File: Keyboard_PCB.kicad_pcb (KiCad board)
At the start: 2 copper layers, 21 parts, among them CON1 PS/2_JACK, CON2 USB_JACK, IC1 FT232RL, U1 ATMEGA328, X1 CRYSTAL

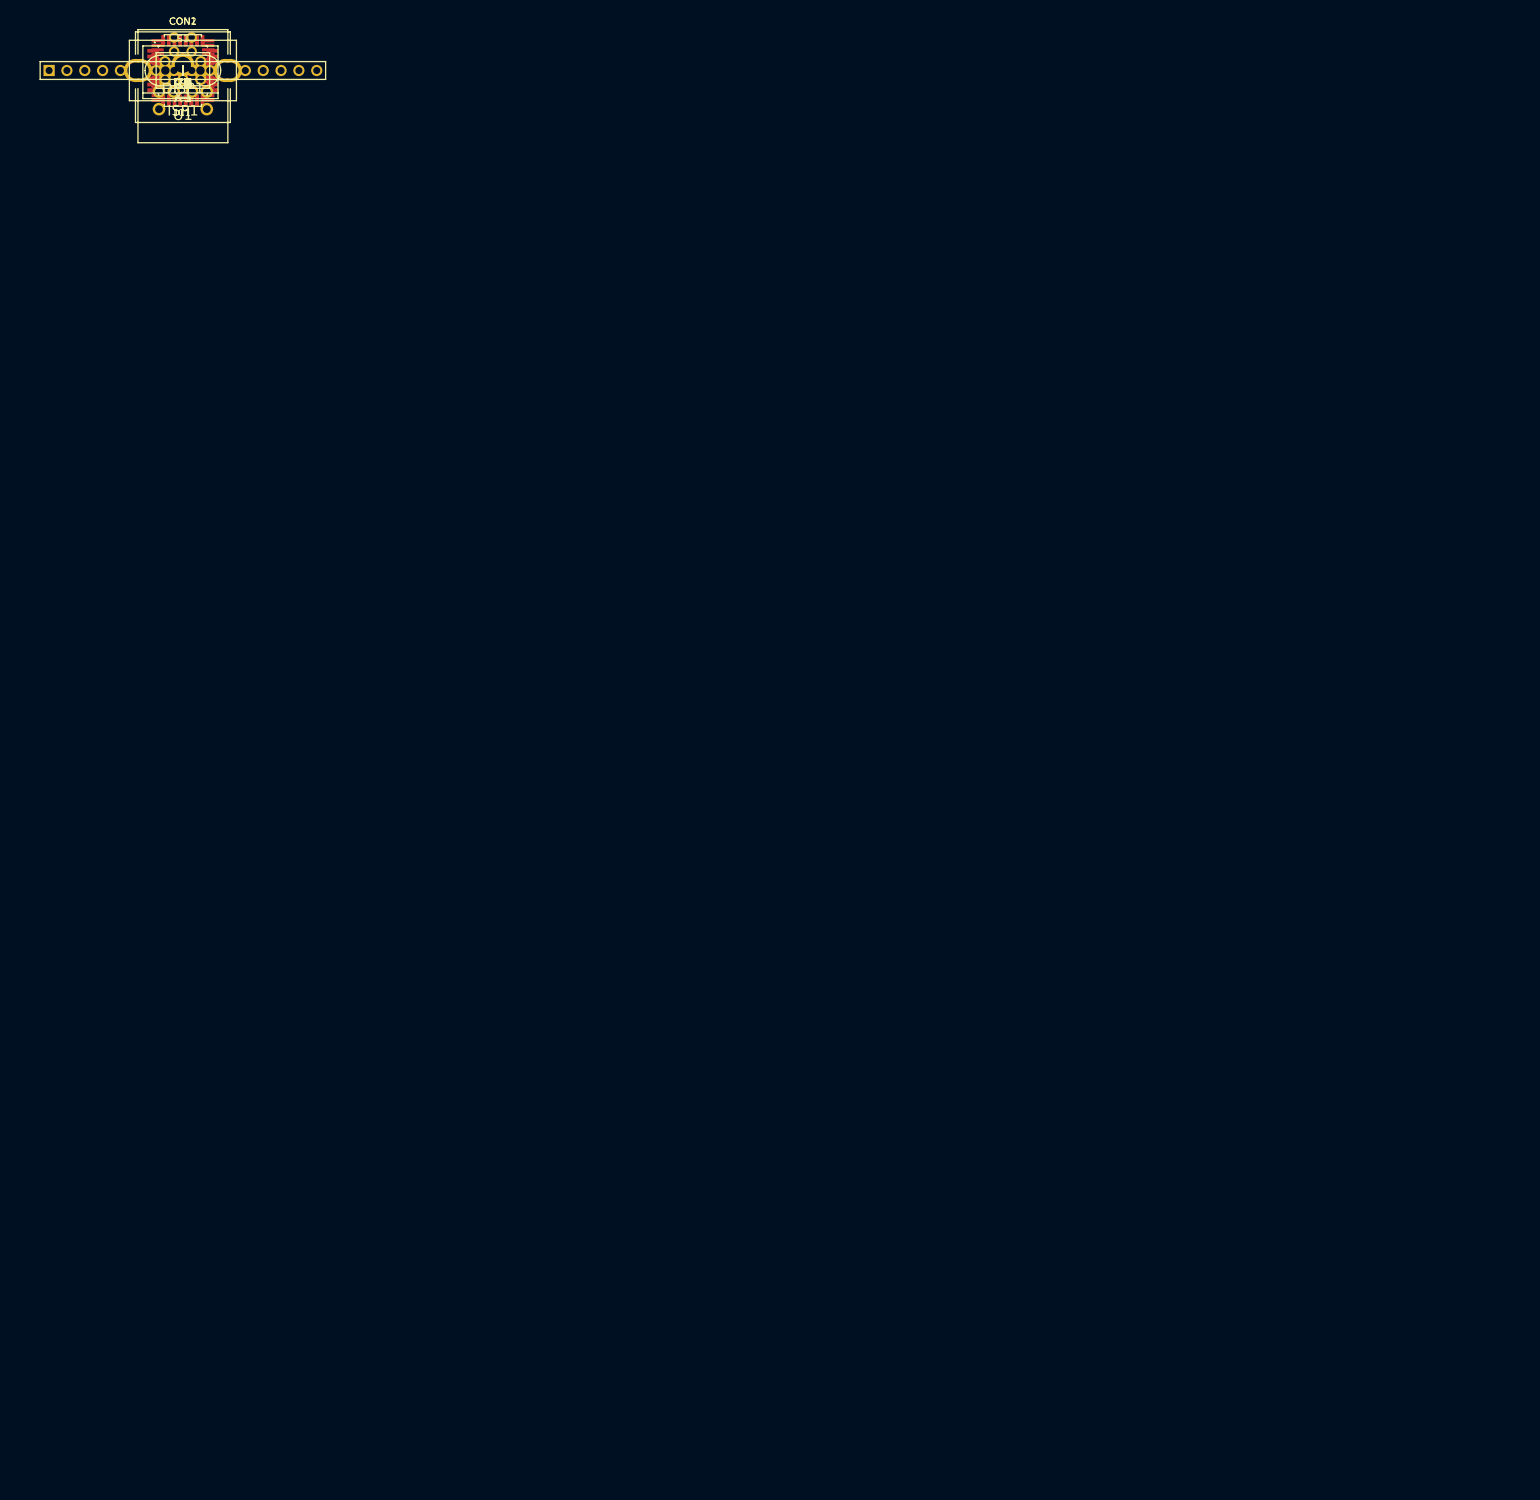
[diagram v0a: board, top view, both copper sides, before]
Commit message: Finished assining Footprints to the schematic symbols.
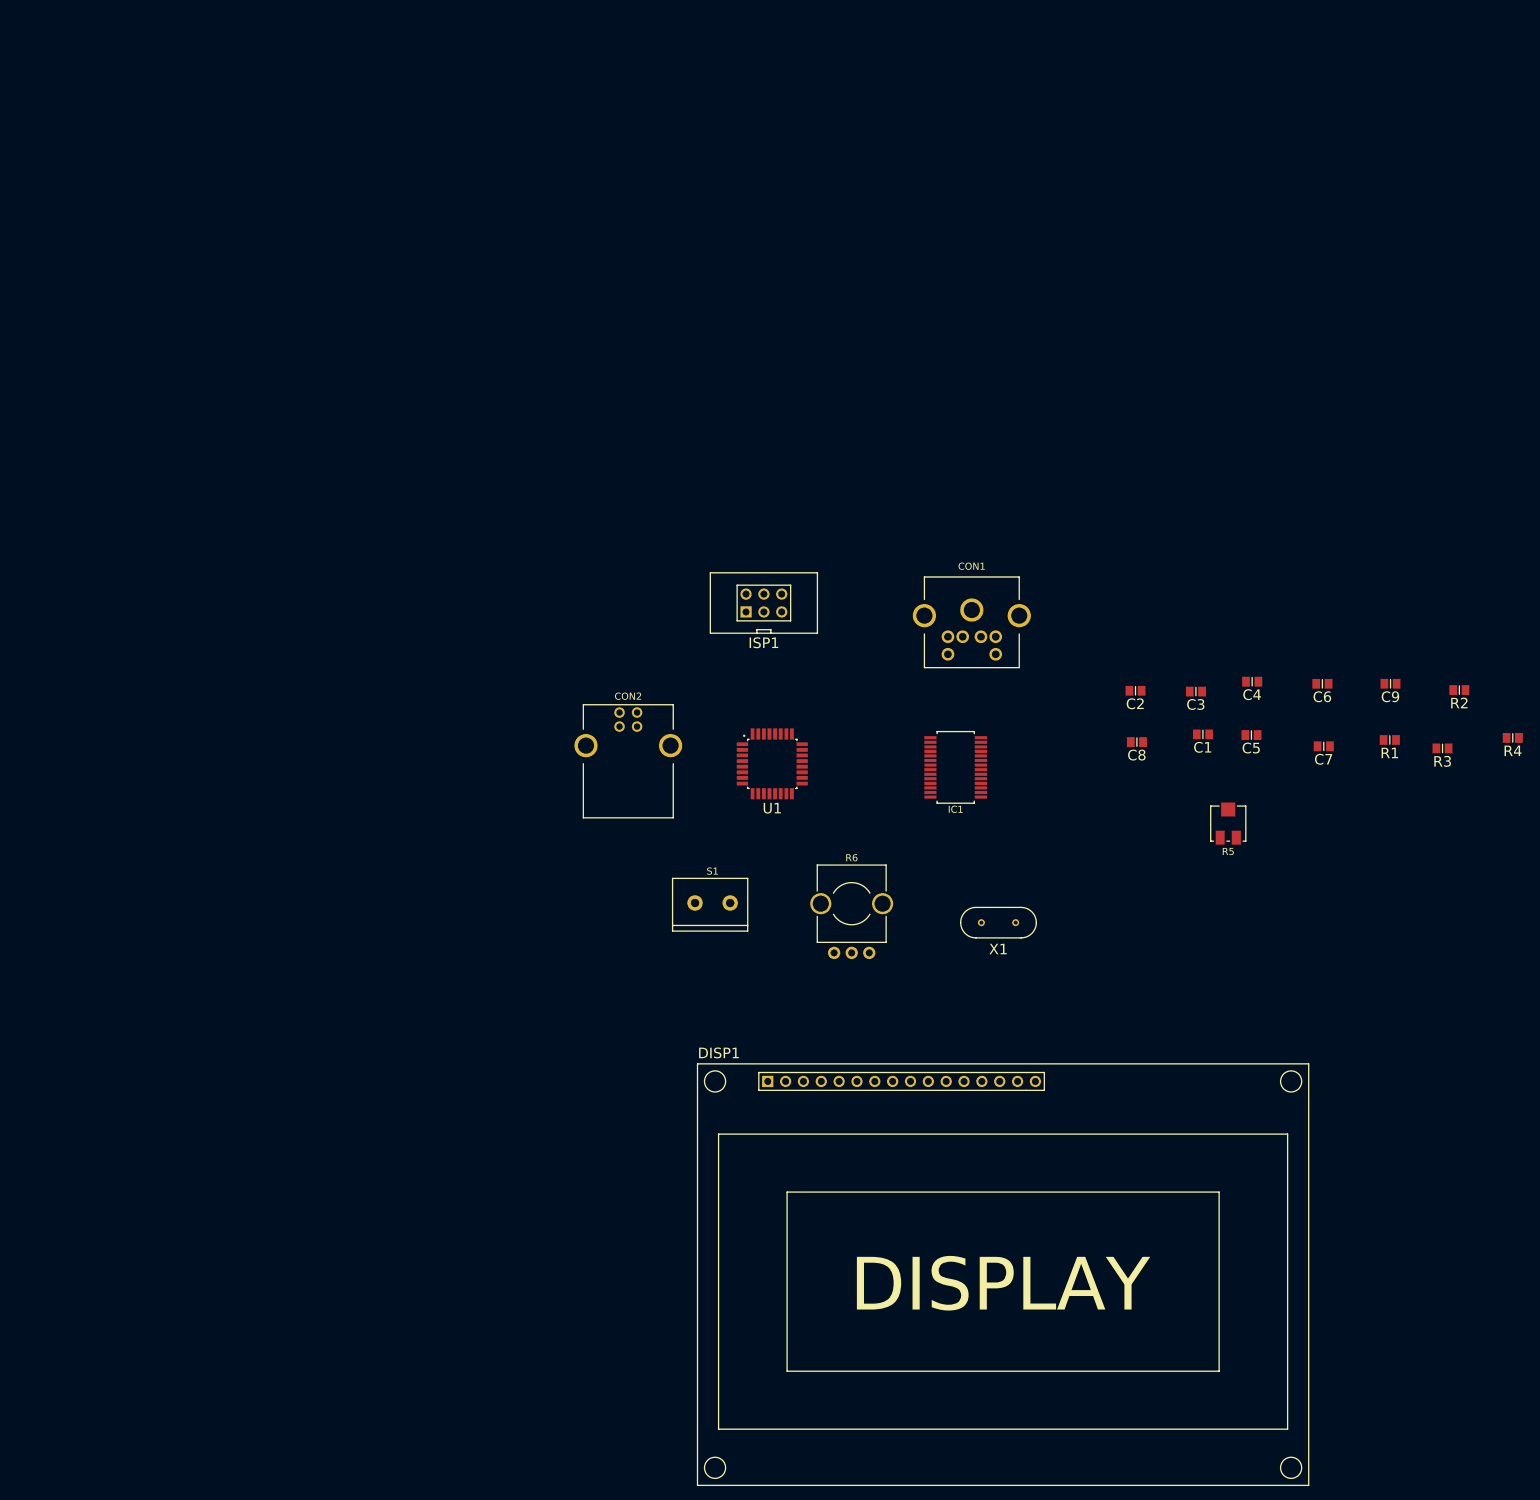
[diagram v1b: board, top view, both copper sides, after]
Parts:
- added R5: RESISTOR_VAR, TRIMMING_POT_SMD, F.Cu at (258.8, 155.2)
- added R6: RESISTOR_VAR, POT_VERT_6mm_MONO, F.Cu at (205.2, 166.6)
- DISP1: footprint PinArray_2.54mm_16x1 -> LCD_TEXT_16x4
- moved R4 211.8 mm to (299.3, 143.0)
- moved R3 203.6 mm to (289.3, 144.5)
- moved R2 202.0 mm to (291.7, 136.2)
- moved R1 196.5 mm to (281.8, 143.3)
- moved C9 192.8 mm to (281.9, 135.3)
- moved C7 188.8 mm to (272.4, 144.2)
- moved C6 184.2 mm to (272.2, 135.3)
- moved C5 179.1 mm to (262.1, 142.6)
- moved DISP1 176.6 mm to (212.3, 191.9)
- moved C4 175.3 mm to (262.2, 135.0)
- moved C1 173.2 mm to (255.2, 142.5)
- moved C3 169.1 mm to (254.2, 136.4)
- moved X1 167.9 mm to (226.1, 169.3)
- moved C8 166.1 mm to (245.8, 143.6)
- moved C2 161.8 mm to (245.6, 136.3)
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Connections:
- net 3 renamed 2
- CON1 pad 2: (no net) -> N-0000033
- CON1 pad 6: (no net) -> N-0000032
- IC1 pad 10: (no net) -> N-0000048
- IC1 pad 11: (no net) -> N-0000047
- IC1 pad 12: (no net) -> N-0000046
- IC1 pad 13: (no net) -> N-0000044
- IC1 pad 14: (no net) -> N-0000043
- IC1 pad 19: (no net) -> N-0000039
- IC1 pad 22: (no net) -> N-0000045
- IC1 pad 23: (no net) -> N-0000038
- IC1 pad 24: (no net) -> N-0000042
- IC1 pad 27: (no net) -> N-0000041
- IC1 pad 28: (no net) -> N-0000040
- IC1 pad 3: (no net) -> N-0000034
- IC1 pad 6: (no net) -> N-0000051
- IC1 pad 8: (no net) -> N-0000050
- IC1 pad 9: (no net) -> N-0000049
- U1 pad 11: (no net) -> N-0000030
- U1 pad 20: (no net) -> N-0000031
- U1 pad 22: (no net) -> N-0000035

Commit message: Placed and routed signals.
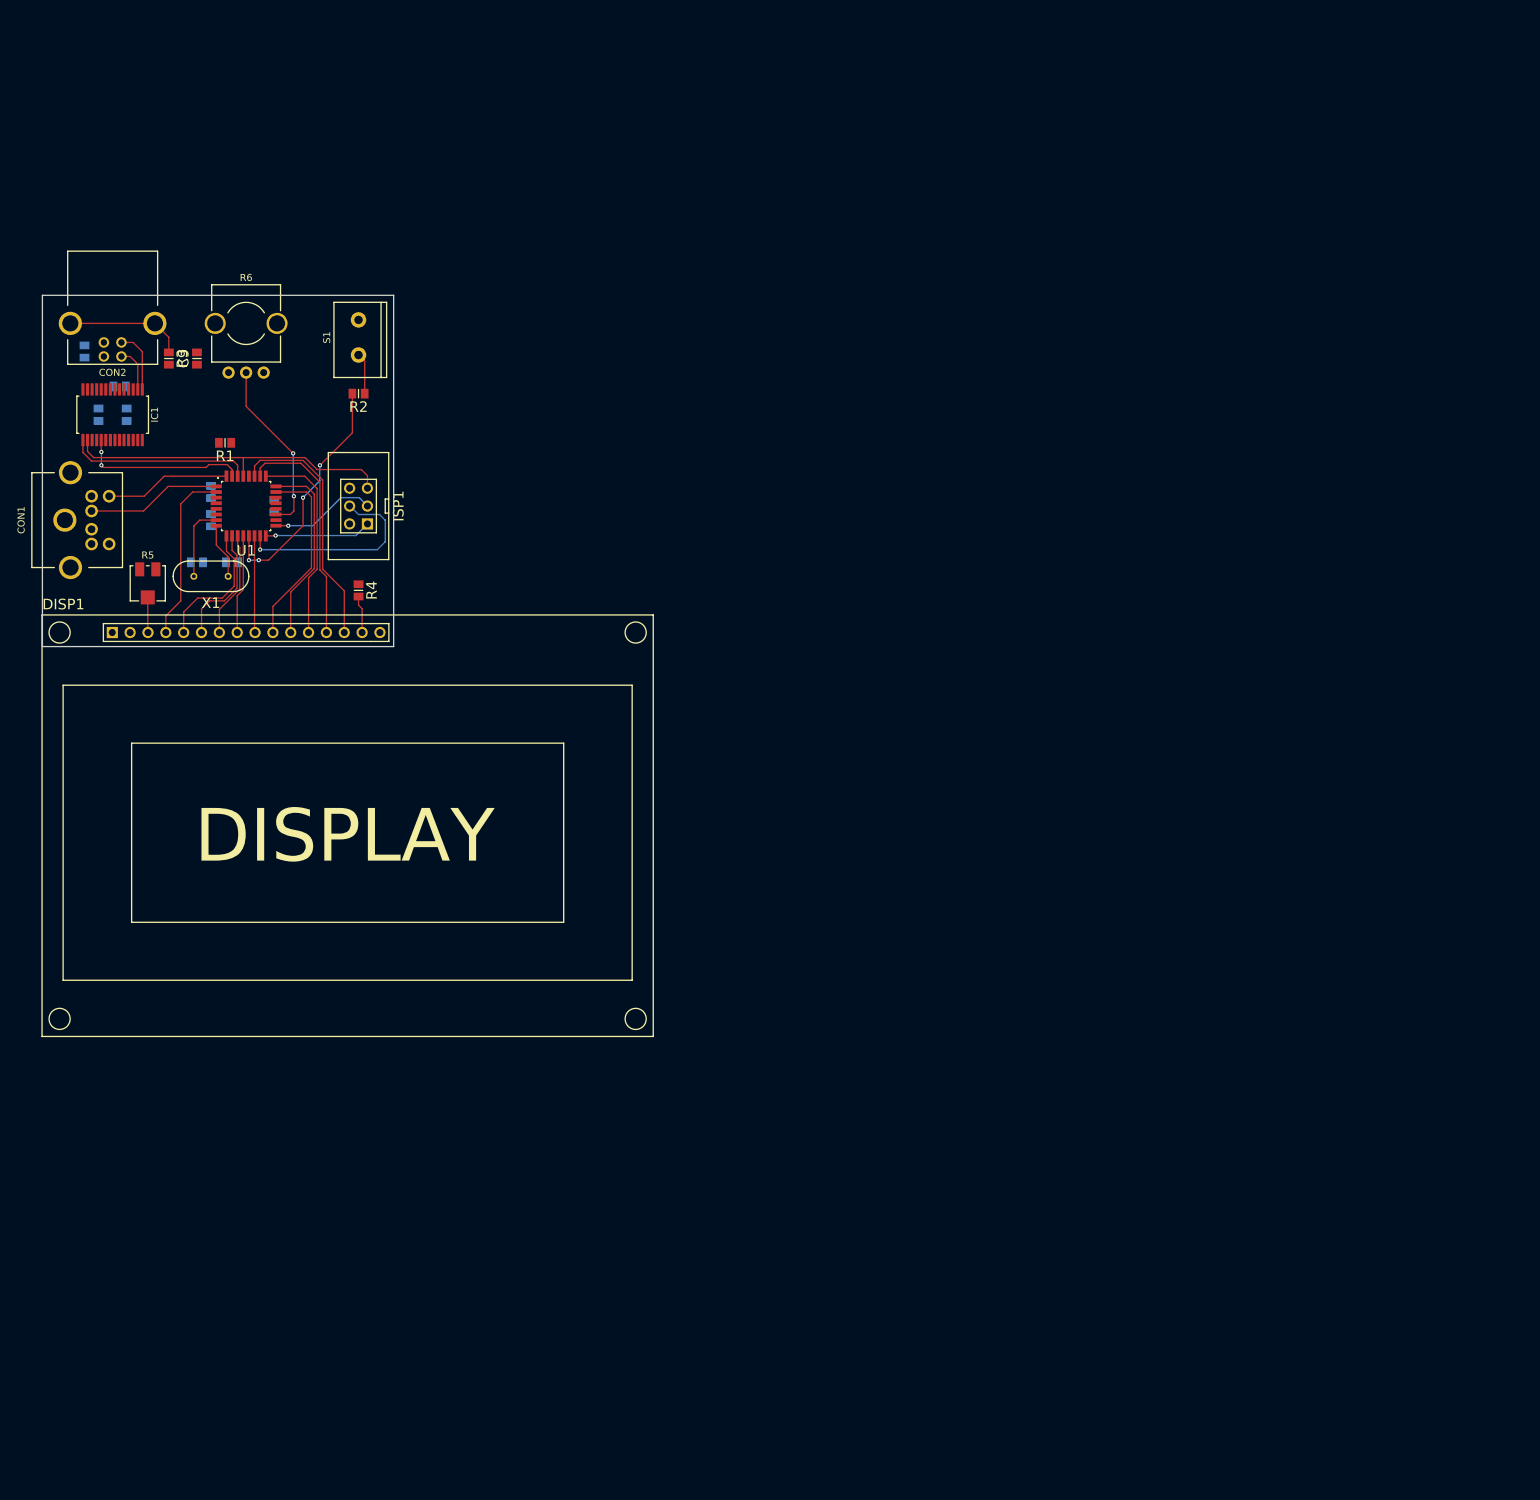
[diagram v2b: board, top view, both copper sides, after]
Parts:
- added C10: CAPACITOR, 0805, B.Cu at (123.0, 110.0)
- C1, C2, C3, C4, C5, C6, C7, C8: moved to B.Cu
- moved R3 189.6 mm to (108.0, 89.0), turned to 90 degrees
- moved C6 178.4 mm to (98.0, 97.0), turned to 90 degrees
- moved C7 176.8 mm to (102.0, 97.0), turned to 90 degrees
- moved C9 176.1 mm to (112.0, 89.0), turned to 270 degrees
- moved R1 171.1 mm to (116.0, 101.0)
- moved C5 168.6 mm to (101.0, 93.0)
- moved R4 165.6 mm to (135.0, 122.0), turned to 90 degrees
- moved R2 162.3 mm to (135.0, 94.0)
- moved C8 159.8 mm to (96.0, 88.0), turned to 90 degrees
- moved R5 157.6 mm to (105.0, 121.0), turned to 180 degrees
- moved C4 150.0 mm to (114.0, 112.0), turned to 270 degrees
- moved C1 145.3 mm to (112.0, 118.0), turned to 180 degrees
- moved C3 143.0 mm to (114.0, 108.0), turned to 90 degrees
- moved IC1 130.1 mm to (100.0, 97.0), turned to 90 degrees
- moved C2 129.9 mm to (117.0, 118.0)
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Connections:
- CON1 pad 2: N-0000033 -> (no net)
- CON1 pad 6: N-0000032 -> (no net)
- DISP1 pad 3: 2 -> N-0000014
- IC1 pad 10: N-0000048 -> (no net)
- IC1 pad 11: N-0000047 -> (no net)
- IC1 pad 12: N-0000046 -> (no net)
- IC1 pad 13: N-0000044 -> (no net)
- IC1 pad 14: N-0000043 -> (no net)
- IC1 pad 19: N-0000039 (its old number) -> (no net)
- IC1 pad 22: N-0000045 -> (no net)
- IC1 pad 23: N-0000038 (its old number) -> (no net)
- IC1 pad 24: N-0000042 -> (no net)
- IC1 pad 27: N-0000041 -> (no net)
- IC1 pad 28: N-0000040 -> (no net)
- IC1 pad 3: N-0000034 -> (no net)
- IC1 pad 6: N-0000051 -> (no net)
- IC1 pad 8: N-0000050 -> (no net)
- IC1 pad 9: N-0000049 -> (no net)
- R5 pad 2: 2 -> N-0000014
- R6 pad 2: 2 -> N-0000018
- U1 pad 10: LCD_RS -> LCD_E
- U1 pad 11: N-0000030 (its old number) -> LCD_D0
- U1 pad 12: LCD_D7 -> LCD_D1
- U1 pad 14: LCD_D6 -> LCD_D2
- U1 pad 19: 2 -> N-0000018
- U1 pad 2: LCD_E -> LCD_RS
- U1 pad 22: N-0000035 -> (no net)
- U1 pad 23: LCD_D5 -> LCD_D3
- U1 pad 25: LCD_D3 -> LCD_D5
- U1 pad 26: LCD_D2 -> LCD_D6
- U1 pad 27: LCD_D1 -> LCD_D7
- U1 pad 28: LCD_D0 -> (no net)
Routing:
- net RESET: track 0.00 -> 47.4 mm
- net LCD_D7: track 0.00 -> 35.6 mm
- net N-000006: track 0.00 -> 34.9 mm, vias 0 -> 4
- net LCD_D6: track 0.00 -> 32.8 mm
- net MOSI: track 0.00 -> 29.2 mm, vias 0 -> 1
- net LCD_D5: track 0.00 -> 29.0 mm
- net LCD_D4: track 0.00 -> 27.0 mm
- net LCD_D3: track 0.00 -> 26.9 mm
- net USB_TX: track 0.00 -> 26.1 mm
- net N-0000018: track 0.00 -> 25.3 mm, vias 0 -> 2
- net LCD_RS: track 0.00 -> 24.9 mm
- net USB_RX: track 0.00 -> 23.7 mm, vias 0 -> 2
- net LCD_RW: track 0.00 -> 19.2 mm
- net N-0000012: track 0.00 -> 19.2 mm
- net N-0000010: track 0.00 -> 17.9 mm
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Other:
- board outline added: 50 x 50 mm
- net class Default: clearance 0.254 -> 0.15; trace_width 0.254 -> 0.15; via_dia 0.889 -> 0.6; via_drill 0.635 -> 0.3
- rule trace_clearance: 0.254 -> 0.15
- rule trace_min: 0.254 -> 0.15
- rule via_min_drill: 0.508 -> 0.3
- rule via_min_size: 0.889 -> 0.6
